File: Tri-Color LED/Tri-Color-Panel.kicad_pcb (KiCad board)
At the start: 2 copper layers, 123.8 x 31.8 mm, 44 parts

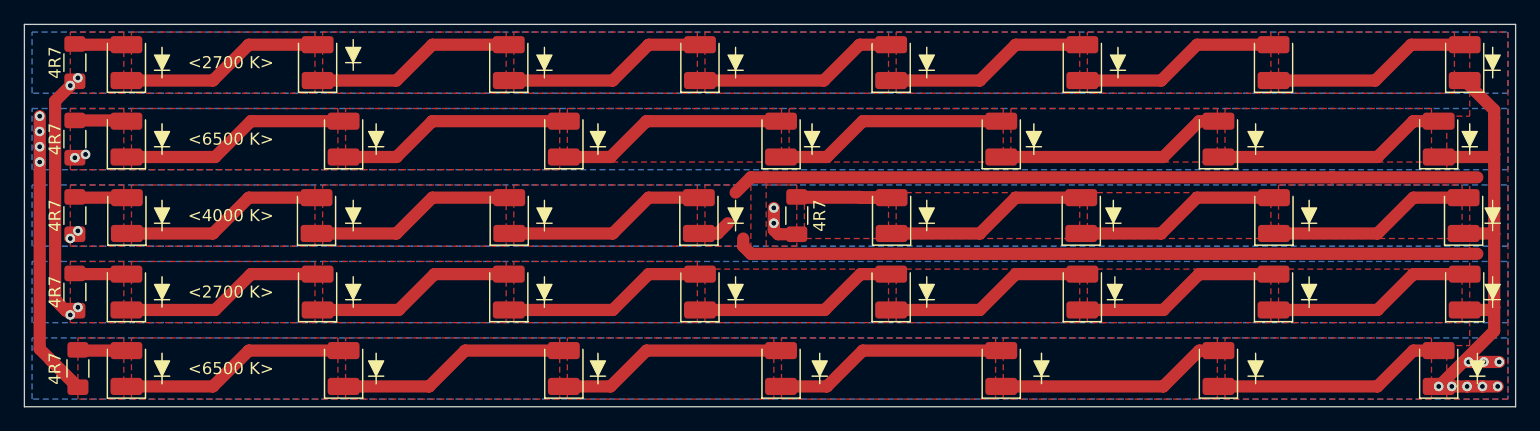
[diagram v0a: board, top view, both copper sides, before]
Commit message: Updated LED to CREE Footprint
Previous footprint is passable; Soldering is inconvenient.
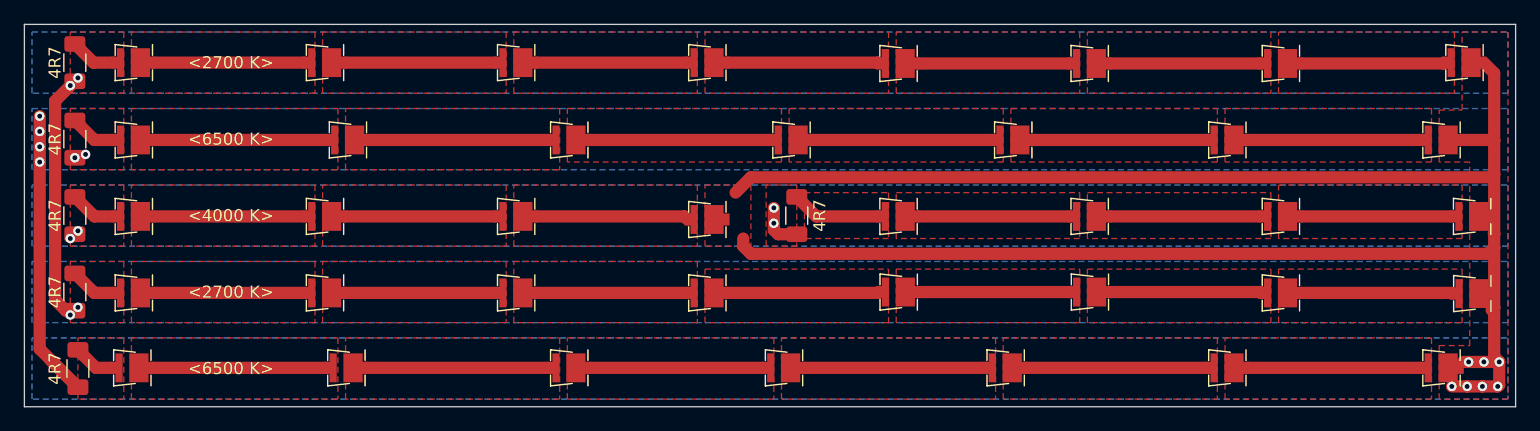
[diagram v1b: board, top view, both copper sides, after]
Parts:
- D1, D10, D11, D12, D13, D14, D15, D16, D17, D18, D19, D2, D20, D21, D22, D23, D24, D25, D26, D27, D28, D29, D3, D30, D31, D32, D33, D34, D35, D36, D37, D38, D4, D5, D6, D7, D8, D9: footprint Diode_SMD:D_1210_3225Metric_Pad1.42x2.65mm_HandSolder -> LED_Cust:LED_CREE_J_3030
- moved D29 3.57 mm to (181.4, 101.2), turned to 180 degrees
- moved D25 3.56 mm to (108.2, 101.2), turned to 180 degrees
- moved D30 3.56 mm to (199.1, 101.2), turned to 180 degrees
- moved D27 3.56 mm to (144.5, 101.2), turned to 180 degrees
- moved D28 3.56 mm to (162.9, 101.2), turned to 180 degrees
- moved D24 3.56 mm to (90.4, 101.2), turned to 180 degrees
- moved D26 3.56 mm to (126.7, 101.2), turned to 180 degrees
- moved D8 3.53 mm to (201.0, 75.9), turned to 180 degrees
- moved D14 3.50 mm to (169.9, 94.9), turned to 180 degrees
- moved D13 3.50 mm to (154.1, 94.9), turned to 180 degrees
- moved D1 3.50 mm to (90.6, 75.9), turned to 180 degrees
- moved D2 3.50 mm to (106.4, 75.9), turned to 180 degrees
- moved D3 3.50 mm to (122.3, 75.9), turned to 180 degrees
- moved D4 3.50 mm to (138.2, 75.9), turned to 180 degrees
- moved D21 3.47 mm to (163.6, 82.3), turned to 180 degrees
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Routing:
- net Net-(D35-Pad2): track 15.8 -> 7.56 mm
- net Net-(D16-Pad1): track 172.8 -> 164.5 mm, vias 8 -> 7
- net Net-(D7-Pad1): track 17.1 -> 12.0 mm
- net Net-(D29-Pad1): track 19.5 -> 14.5 mm
- net Net-(D22-Pad1): track 19.5 -> 14.5 mm
- net Net-(D24-Pad1): track 19.3 -> 14.5 mm
- net Net-(D21-Pad1): track 19.3 -> 14.5 mm
- net Net-(D17-Pad1): track 19.3 -> 14.5 mm
- net Net-(D26-Pad1): track 19.3 -> 14.6 mm
- net Net-(D36-Pad1): track 17.2 -> 12.6 mm
- net Net-(D32-Pad1): track 17.2 -> 12.6 mm
- net Net-(D6-Pad1): track 17.1 -> 12.6 mm
- net Net-(D5-Pad1): track 17.1 -> 12.6 mm
- net Net-(D2-Pad1): track 17.1 -> 12.6 mm
- net Net-(D10-Pad2): track 17.1 -> 12.6 mm
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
